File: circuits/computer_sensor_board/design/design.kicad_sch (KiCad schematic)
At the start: 3 parts, among them J1 Conn_01x02, U1 TDN_5-2411WISM, U2 Teensy4.1

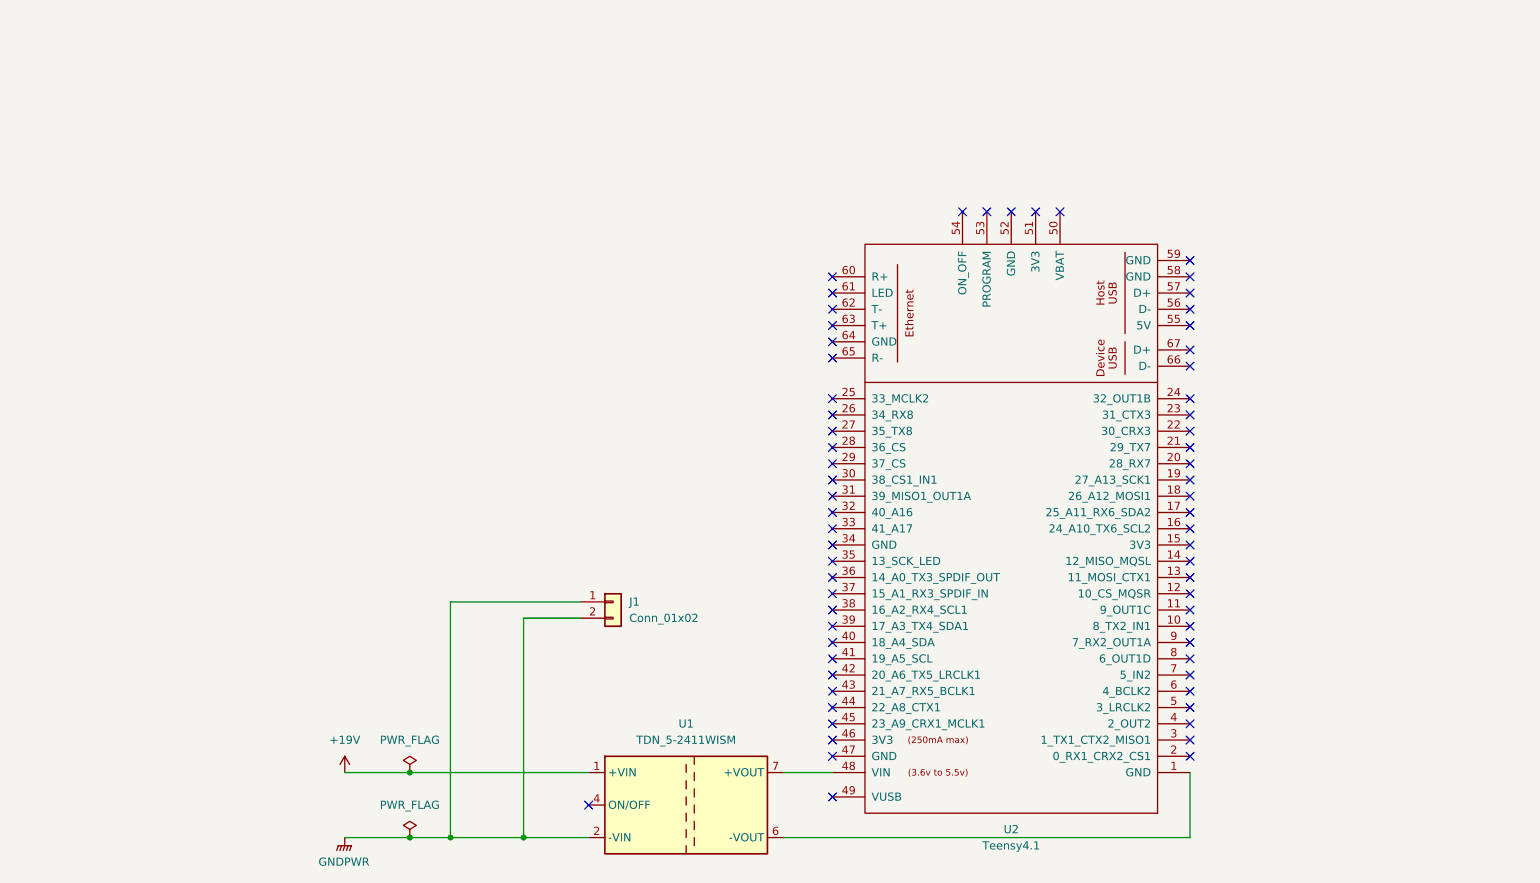
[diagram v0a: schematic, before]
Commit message: enable save schematic in SVG
Signed-off-by: Masaya Kataoka <ms.kataoka@gmail.com>
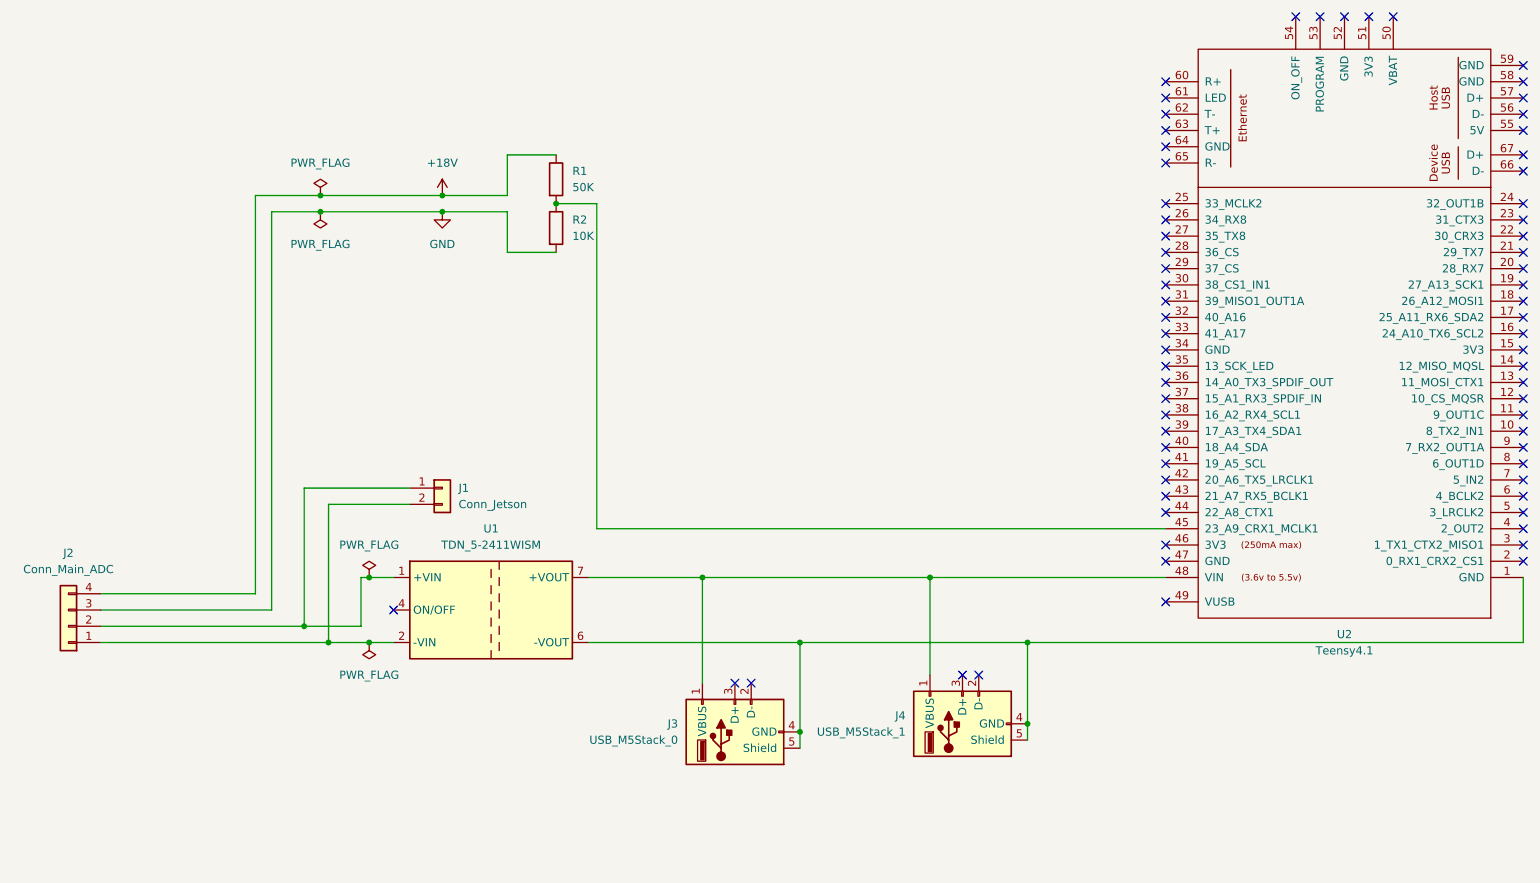
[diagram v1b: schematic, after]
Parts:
- added J2: Conn_Main_ADC, symbol Connector_Generic:Conn_01x04
- added J3: USB_M5Stack_0, symbol Connector:USB_A
- added J4: USB_M5Stack_1, symbol Connector:USB_A
- added R1: 50K, symbol Device:R
- added R2: 10K, symbol Device:R
- J1: value Conn_01x02 -> Conn_Jetson
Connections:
- net at U1.6 (-VOUT), U2.1 (GND): now also J3.4 (GND), J3.5 (Shield), J4.4 (GND), J4.5 (Shield)
- net at U1.7 (+VOUT), U2.48 (VIN): now also J3.1 (VBUS), J4.1 (VBUS)
- net at U2.45 (23_A9_CRX1_MCLK1): now also R1.2, R2.1
- net +19V: no longer names the net of U1.1 (+VIN)
- net +19V: now also J1.1 (Pin_1), J2.2 (Pin_2)
- net GNDPWR: no longer names the net of J1.2 (Pin_2), U1.2 (-VIN)
- net GNDPWR: now also J2.1 (Pin_1); no longer J1.1 (Pin_1)
- new net +18V: J2.4 (Pin_4), R1.1
- new net GND: J2.3 (Pin_3), R2.2
- no-connect marks 66 -> 69
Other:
- moved on the sheet: J1, U1, U2
